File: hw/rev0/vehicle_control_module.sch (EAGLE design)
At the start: 486 parts, among them IC1 SJA1105TELY, IC10 TJA1100HNZ, IC11 KSZ8061MNXI-TR, IC12 TJA1100HNZ, IC13 TLE9250XSJXUMA1, IC17 LP5907QMFX-3.3Q1, IC18 TLE9250XSJXUMA1, IC2 ATSAMV71Q21B-AABT, IC3 TJA1100HNZ, IC4 FT2232HL, IC5 TRS3232EQPWRQ1, IC6 SST26VF032BT-104I_SM, IC7 DS3231SN#, IC8 74HC7541D-Q100J, IC9 TPS62242DRVR, J10 5-2337992-3, J11 2301843-1, J12 1017505, J13 2301843-1, J15 693022010811, J2 2305018-2, J27 2041119-2, J3 1017505, J4 1017505, J5 1017505, J6 1017505, J7 1017505, J8 1017505, J9 1017505, U1 122-2920-GR, U2 LM63625, U3 TPS62007-Q1_DGS_10, Y1 NX3225SA-25MHZ-EXS00A-CS11338, Y3 ABM8AIG-12.000MHZ-1Z-T

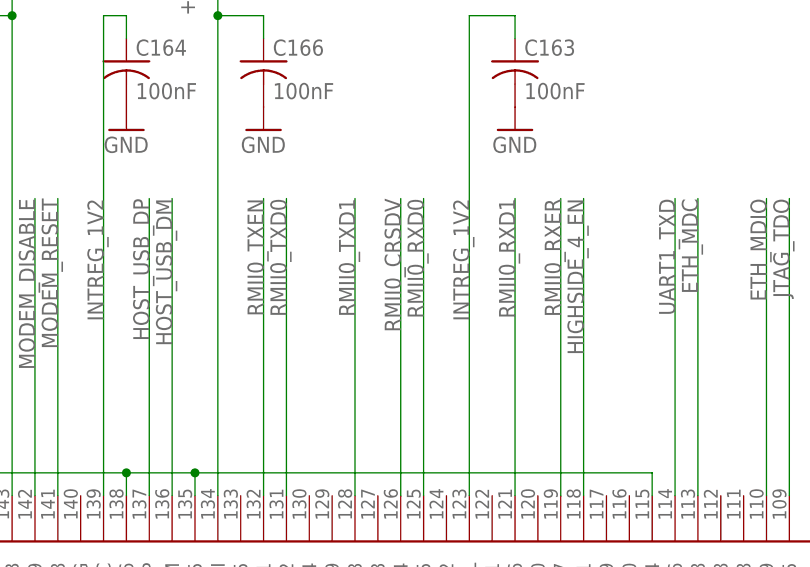
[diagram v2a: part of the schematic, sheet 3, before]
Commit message: Fix connection between MCU and switch
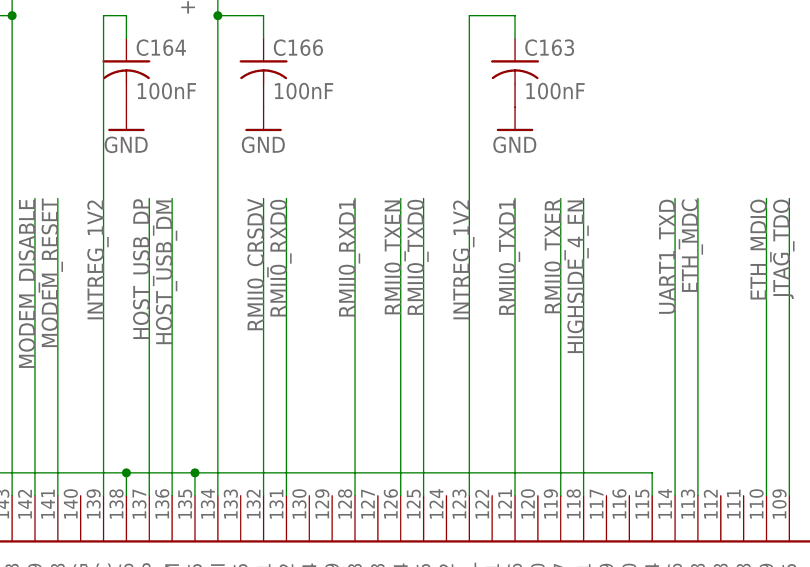
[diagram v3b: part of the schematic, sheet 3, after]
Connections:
- removed net RMII0_RXER: IC1.MII0_RX_ER, IC2.PD7
- new net RMII0_TXER: IC1.MII0_TX_ER, IC2.PD7
- net RMII0_CRSDV: now also IC2.PD1; no longer IC2.PD4
- net RMII0_RXD0: now also IC2.PD2; no longer IC2.PD5
- net RMII0_RXD1: now also IC2.PD3; no longer IC2.PD6
- net RMII0_TXD0: now also IC2.PD5; no longer IC2.PD2
- net RMII0_TXD1: now also IC2.PD6; no longer IC2.PD3
- net RMII0_TXEN: now also IC2.PD4; no longer IC2.PD1
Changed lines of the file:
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@@
 <grid distance="0.1" unitdist="inch" unit="inch" style="lines" multiple="1" display="no" altdistance="0.01" altunitdist="inch" altunit="inch"/>
 <layers>
-<layer number="1" name="Top" color="4" fill="1" visible="yes" active="no"/>
-<layer number="2" name="Route2" color="16" fill="1" visible="yes" active="no"/>
-<layer number="3" name="Route3" color="17" fill="1" visible="yes" active="no"/>
-<layer number="4" name="Route4" color="18" fill="1" visible="yes" active="no"/>
-<layer number="5" name="Route5" color="19" fill="1" visible="yes" active="no"/>
-<layer number="6" name="Route6" color="25" fill="1" visible="yes" active="no"/>
-<layer number="7" name="Route7" color="26" fill="1" visible="yes" active="no"/>
-<layer number="8" name="Route8" color="27" fill="1" visible="yes" active="no"/>
-<layer number="9" name="Route9" color="28" fill="1" visible="yes" active="no"/>
-<layer number="10" name="Route10" color="29" fill="1" visible="yes" active="no"/>
-<layer number="11" name="Route11" color="30" fill="1" visible="yes" active="no"/>
-<layer number="12" name="Route12" color="20" fill="1" visible="yes" active="no"/>
-<layer number="13" name="Route13" color="21" fill="1" visible="yes" active="no"/>
-<layer number="14" name="Route14" color="22" fill="1" visible="yes" active="no"/>
-<layer number="15" name="Route15" color="23" fill="1" visible="yes" active="no"/>
-<layer number="16" name="Bottom" color="1" fill="1" visible="yes" active="no"/>
-<layer number="17" name="Pads" color="2" fill="1" visible="yes" active="no"/>
-<layer number="18" name="Vias" color="2" fill="1" visible="yes" active="no"/>
-<layer number="19" name="Unrouted" color="6" fill="1" visible="yes" active="no"/>
-<layer number="20" name="Dimension" color="24" fill="1" visible="yes" active="no"/>
-<layer number="21" name="tPlace" color="7" fill="1" visible="yes" active="no"/>
-<layer number="22" name="bPlace" color="7" fill="1" visible="yes" active="no"/>
-<layer number="23" name="tOrigins" color="15" fill="1" visible="yes" active="no"/>
-<layer number="24" name="bOrigins" color="15" fill="1" visible="yes" active="no"/>
-<layer number="25" name="tNames" color="7" fill="1" visible="yes" active="no"/>
-<layer number="26" name="bNames" color="7" fill="1" visible="yes" active="no"/>
-<layer number="27" name="tValues" color="7" fill="1" visible="yes" active="no"/>
-<layer number="28" name="bValues" color="7" fill="1" visible="yes" active="no"/>
+<layer number="1" name="Top" color="4" fill="1" visible="no" active="no"/>
+<layer number="2" name="Route2" color="16" fill="1" visible="no" active="no"/>
+<layer number="3" name="Route3" color="17" fill="1" visible="no" active="no"/>
+<layer number="4" name="Route4" color="18" fill="1" visible="no" active="no"/>
+<layer number="5" name="Route5" color="19" fill="1" visible="no" active="no"/>
+<layer number="6" name="Route6" color="25" fill="1" visible="no" active="no"/>
+<layer number="7" name="Route7" color="26" fill="1" visible="no" active="no"/>
+<layer number="8" name="Route8" color="27" fill="1" visible="no" active="no"/>
+<layer number="9" name="Route9" color="28" fill="1" visible="no" active="no"/>
+<layer number="10" name="Route10" color="29" fill="1" visible="no" active="no"/>
+<layer number="11" name="Route11" color="30" fill="1" visible="no" active="no"/>
+<layer number="12" name="Route12" color="20" fill="1" visible="no" active="no"/>
+<layer number="13" name="Route13" color="21" fill="1" visible="no" active="no"/>
+<layer number="14" name="Route14" color="22" fill="1" visible="no" active="no"/>
+<layer number="15" name="Route15" color="23" fill="1" visible="no" active="no"/>
+<layer number="16" name="Bottom" color="1" fill="1" visible="no" active="no"/>
+<layer number="17" name="Pads" color="2" fill="1" visible="no" active="no"/>
+<layer number="18" name="Vias" color="2" fill="1" visible="no" active="no"/>
+<layer number="19" name="Unrouted" color="6" fill="1" visible="no" active="no"/>
+<layer number="20" name="Dimension" color="24" fill="1" visible="no" active="no"/>
+<layer number="21" name="tPlace" color="7" fill="1" visible="no" active="no"/>
+<layer number="22" name="bPlace" color="7" fill="1" visible="no" active="no"/>
+<layer number="23" name="tOrigins" color="15" fill="1" visible="no" active="no"/>
+<layer number="24" name="bOrigins" color="15" fill="1" visible="no" active="no"/>
+<layer number="25" name="tNames" color="7" fill="1" visible="no" active="no"/>
+<layer number="26" name="bNames" color="7" fill="1" visible="no" active="no"/>
+<layer number="27" name="tValues" color="7" fill="1" visible="no" active="no"/>
+<layer number="28" name="bValues" color="7" fill="1" visible="no" active="no"/>
 <layer number="29" name="tStop" color="7" fill="3" visible="no" active="no"/>
 <layer number="30" name="bStop" color="7" fill="6" visible="no" active="no"/>
@@
 <layer number="35" name="tGlue" color="7" fill="4" visible="no" active="no"/>
 <layer number="36" name="bGlue" color="7" fill="5" visible="no" active="no"/>
-<layer number="37" name="tTest" color="7" fill="1" visible="yes" active="no"/>
-<layer number="38" name="bTest" color="7" fill="1" visible="yes" active="no"/>
+<layer number="37" name="tTest" color="7" fill="1" visible="no" active="no"/>
+<layer number="38" name="bTest" color="7" fill="1" visible="no" active="no"/>
 <layer number="39" name="tKeepout" color="4" fill="11" visible="no" active="no"/>
 <layer number="40" name="bKeepout" color="1" fill="11" visible="no" active="no"/>
@@
 <layer number="44" name="Drills" color="7" fill="1" visible="no" active="no"/>
 <layer number="45" name="Holes" color="7" fill="1" visible="no" active="no"/>
-<layer number="46" name="Milling" color="3" fill="1" visible="yes" active="no"/>
-<layer number="47" name="Measures" color="7" fill="1" visible="yes" active="no"/>
-<layer number="48" name="Document" color="7" fill="1" visible="yes" active="no"/>
-<layer number="49" name="Reference" color="7" fill="1" visible="yes" active="no"/>
-<layer number="50" name="dxf" color="7" fill="1" visible="yes" active="no"/>
-<layer number="51" name="tDocu" color="7" fill="1" visible="yes" active="no"/>
-<layer number="52" name="bDocu" color="7" fill="1" visible="yes" active="no"/>
+<layer number="46" name="Milling" color="3" fill="1" visible="no" active="no"/>
+<layer number="47" name="Measures" color="7" fill="1" visible="no" active="no"/>
+<layer number="48" name="Document" color="7" fill="1" visible="no" active="no"/>
+<layer number="49" name="Reference" color="7" fill="1" visible="no" active="no"/>
+<layer number="50" name="dxf" color="7" fill="1" visible="no" active="no"/>
+<layer number="51" name="tDocu" color="7" fill="1" visible="no" active="no"/>
+<layer number="52" name="bDocu" color="7" fill="1" visible="no" active="no"/>
 <layer number="88" name="SimResults" color="9" fill="1" visible="yes" active="yes"/>
 <layer number="89" name="SimProbes" color="9" fill="1" visible="yes" active="yes"/>
@@
 </segment>
 </net>
-<net name="RMII0_RXER" class="0">
+<net name="RMII0_TXER" class="0">
 <segment>
 <pinref part="IC2" gate="G$1" pin="PD7"/>
@@
 </segment>
 </net>
-<net name="RMII0_RXD1" class="0">
+<net name="RMII0_TXD1" class="0">
 <segment>
 <pinref part="IC2" gate="G$1" pin="PD6"/>
@@
 </segment>
 </net>
-<net name="RMII0_RXD0" class="0">
+<net name="RMII0_TXD0" class="0">
 <segment>
 <pinref part="IC2" gate="G$1" pin="PD5"/>
@@
 </segment>
 </net>
-<net name="RMII0_CRSDV" class="0">
+<net name="RMII0_TXEN" class="0">
 <segment>
 <pinref part="IC2" gate="G$1" pin="PD4"/>
@@
 </segment>
 </net>
-<net name="RMII0_TXD1" class="0">
-<segment>
-<pinref part="IC2" gate="G$1" pin="PD3"/>
-<wire x1="157.48" y1="198.12" x2="157.48" y2="231.14" width="0.1524" layer="91"/>
-<label x="157.48" y="231.14" size="1.778" layer="95" rot="MR270"/>
-</segment>
-</net>
-<net name="RMII0_TXD0" class="0">
-<segment>
-<pinref part="IC2" gate="G$1" pin="PD2"/>
-<wire x1="149.86" y1="198.12" x2="149.86" y2="231.14" width="0.1524" layer="91"/>
-<label x="149.86" y="231.14" size="1.778" layer="95" rot="MR270"/>
-</segment>
-</net>
-<net name="RMII0_TXEN" class="0">
-<segment>
-<pinref part="IC2" gate="G$1" pin="PD1"/>
-<wire x1="147.32" y1="198.12" x2="147.32" y2="231.14" width="0.1524" layer="91"/>
-<label x="147.32" y="231.14" size="1.778" layer="95" rot="MR270"/>
-</segment>
-</net>
 <net name="I2C0_TWCK" class="0">
 <segment>
@@
 </segment>
 </net>
+<net name="RMII0_RXD0" class="0">
+<segment>
+<pinref part="IC2" gate="G$1" pin="PD2"/>
+<wire x1="149.86" y1="198.12" x2="149.86" y2="231.14" width="0.1524" layer="91"/>
+<label x="149.86" y="231.14" size="1.778" layer="95" rot="MR270"/>
+</segment>
+</net>
+<net name="RMII0_RXD1" class="0">
+<segment>
+<pinref part="IC2" gate="G$1" pin="PD3"/>
+<wire x1="157.48" y1="198.12" x2="157.48" y2="231.14" width="0.1524" layer="91"/>
+<label x="157.48" y="231.14" size="1.778" layer="95" rot="MR270"/>
+</segment>
+</net>
+<net name="RMII0_CRSDV" class="0">
+<segment>
+<pinref part="IC2" gate="G$1" pin="PD1"/>
+<wire x1="147.32" y1="198.12" x2="147.32" y2="231.14" width="0.1524" layer="91"/>
+<label x="147.32" y="231.14" size="1.778" layer="95" rot="MR270"/>
+</segment>
+</net>
 </nets>
 </sheet>
@@
 </segment>
 </net>
-<net name="RMII0_RXER" class="0">
-<segment>
-<pinref part="IC1" gate="G$1" pin="MII0_RX_ER"/>
-<wire x1="248.92" y1="231.14" x2="284.48" y2="231.14" width="0.1524" layer="91"/>
-<label x="284.48" y="231.14" size="1.778" layer="95" rot="MR0"/>
-</segment>
-</net>
 <net name="RMII0_TXEN" class="0">
 <segment>
@@
 </segment>
 </net>
+<net name="RMII0_TXER" class="0">
+<segment>
+<pinref part="IC1" gate="G$1" pin="MII0_TX_ER"/>
+<wire x1="198.12" y1="226.06" x2="149.86" y2="226.06" width="0.1524" layer="91"/>
+<label x="149.86" y="226.06" size="1.778" layer="95"/>
+</segment>
+</net>
